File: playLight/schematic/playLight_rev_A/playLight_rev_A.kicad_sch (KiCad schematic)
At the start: 30 parts, among them J1 Conn_01x01, J10 Conn_01x01, J2 Conn_01x01, J3 Conn_01x01, J4 Conn_01x01, J5 Conn_01x01, J6 Conn_01x01, J7 Conn_01x01, J8 Conn_01x01, J9 Conn_01x01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

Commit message: added gerbers added PDF export
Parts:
- R1, R2: value R_US -> 2.2k
- R3: value R_US -> 1k
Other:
- company: (none) -> QuBi
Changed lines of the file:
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@@
 	(title_block
 		(title "gangQin Playlight")
+		(date "20 April 2026")
 		(rev "Rev A")
+		(company "QuBi")
 	)
 	(junction
@@
 			)
 		)
-		(property "Value" "R_US"
+		(property "Value" "2.2k"
 			(at 119.38 64.7699 0)
 			(effects
@@
 			)
 		)
-		(property "Value" "R_US"
+		(property "Value" "2.2k"
 			(at 132.08 64.7699 0)
 			(effects
@@
 			)
 		)
-		(property "Value" "R_US"
+		(property "Value" "1k"
 			(at 173.99 180.3399 0)
 			(effects

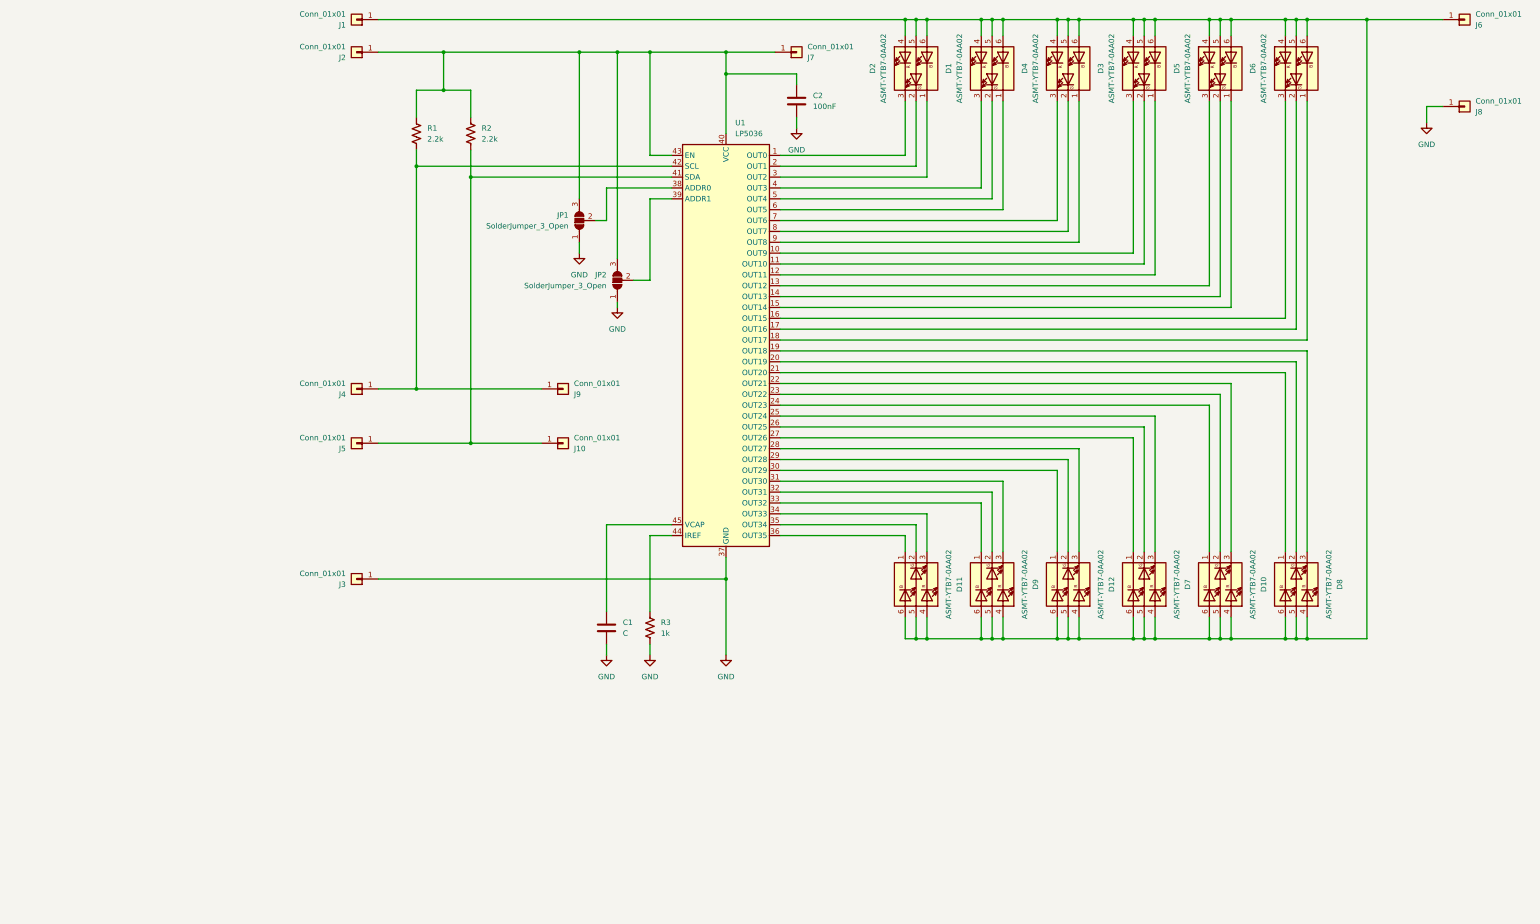
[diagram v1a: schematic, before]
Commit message: added design notes in the schematic minor tweaks in the PCB generated the gerbers accordingly
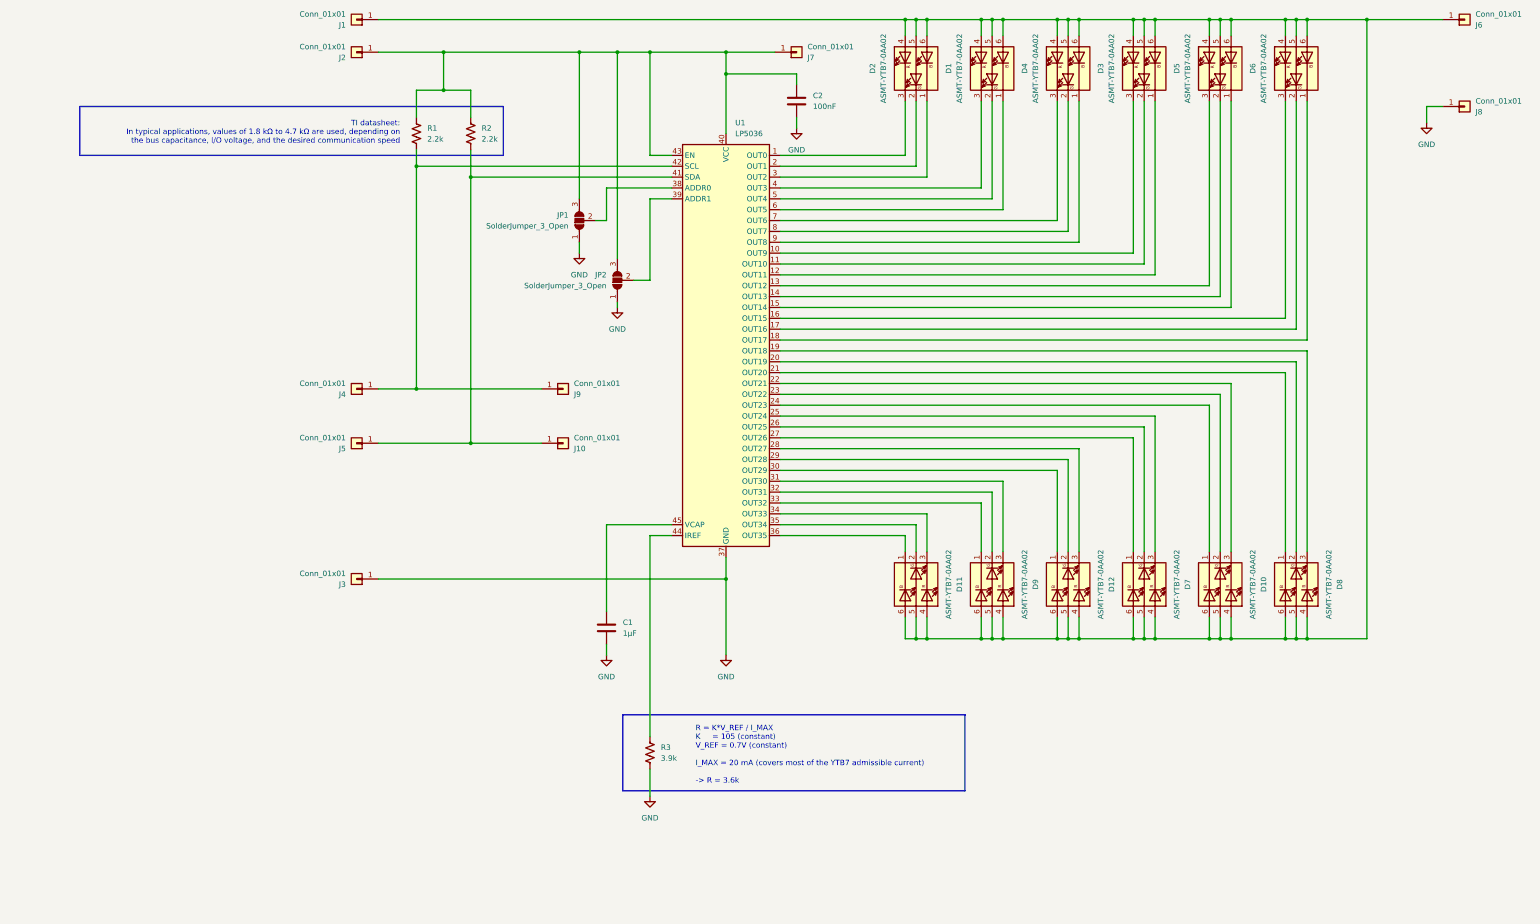
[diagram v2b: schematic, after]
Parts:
- C1: value C -> 1µF
- R3: value 1k -> 3.9k
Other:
- note added: "R = K*V_REF / I_MAX K = 105 (constant) V_REF = 0.7V (constant) I_MAX = 20 mA (covers most of the YTB7 admissible current) -> R = 3.6k"
- note added: "TI datasheet: In typical applications, values of 1.8 kΩ to 4.7 kΩ are used, depending on the bus capacitance, I/O voltage, and the desired communication speed"
- moved on the sheet: R3
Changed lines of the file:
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@@
 		(company "QuBi")
 	)
+	(rectangle
+		(start 38.1 57.15)
+		(end 137.16 68.58)
+		(stroke
+			(width 0)
+			(type default)
+		)
+		(fill
+			(type none)
+		)
+	)
+	(rectangle
+		(start 165.1 199.39)
+		(end 245.11 217.17)
+		(stroke
+			(width 0)
+			(type default)
+		)
+		(fill
+			(type none)
+		)
+	)
+	(text "R = K*V_REF / I_MAX\nK     = 105 (constant)\nV_REF = 0.7V (constant)\n\nI_MAX = 20 mA (covers most of the YTB7 admissible current)\n\n-> R = 3.6k\n"
+		(exclude_from_sim no)
+		(at 182.118 208.788 0)
+		(effects
+			(font
+				(size 1.27 1.27)
+			)
+			(justify left)
+		)
+	)
+	(text "TI datasheet:\nIn typical applications, values of 1.8 kΩ to 4.7 kΩ are used, depending on\nthe bus capacitance, I/O voltage, and the desired communication speed\n"
+		(exclude_from_sim no)
+		(at 113.03 63.246 0)
+		(effects
+			(font
+				(size 1.27 1.27)
+			)
+			(justify right)
+		)
+	)
 	(junction
 		(at 325.12 36.83)
@@
 	(wire
 		(pts
-			(xy 171.45 175.26) (xy 171.45 157.48)
+			(xy 171.45 204.47) (xy 171.45 157.48)
 		)
 		(stroke
@@
 	(wire
 		(pts
-			(xy 171.45 182.88) (xy 171.45 185.42)
+			(xy 171.45 212.09) (xy 171.45 218.44)
 		)
 		(stroke
@@
 	(symbol
 		(lib_id "power:GND")
-		(at 171.45 185.42 0)
+		(at 171.45 218.44 0)
 		(unit 1)
 		(exclude_from_sim no)
@@
 		(fields_autoplaced yes)
 		(property "Reference" "#PWR04"
-			(at 171.45 191.77 0)
+			(at 171.45 224.79 0)
 			(effects
 				(font
@@
 		)
 		(property "Value" "GND"
-			(at 171.45 190.5 0)
+			(at 171.45 223.52 0)
 			(effects
 				(font
@@
 		)
 		(property "Footprint" ""
-			(at 171.45 185.42 0)
+			(at 171.45 218.44 0)
 			(effects
 				(font
@@
 		)
 		(property "Datasheet" ""
-			(at 171.45 185.42 0)
+			(at 171.45 218.44 0)
 			(effects
 				(font
@@
 		)
 		(property "Description" "Power symbol creates a global label with name \"GND\" , ground"
-			(at 171.45 185.42 0)
+			(at 171.45 218.44 0)
 			(effects
 				(font
@@
 			)
 		)
-		(property "Value" "C"
+		(property "Value" "1µF"
 			(at 165.1 180.3399 0)
 			(effects
@@
 	(symbol
 		(lib_id "Device:R_US")
-		(at 171.45 179.07 0)
+		(at 171.45 208.28 0)
 		(unit 1)
 		(exclude_from_sim no)
@@
 		(dnp no)
 		(property "Reference" "R3"
-			(at 173.99 177.7999 0)
+			(at 173.99 207.0099 0)
 			(effects
 				(font
@@
 			)
 		)
-		(property "Value" "1k"
-			(at 173.99 180.3399 0)
+		(property "Value" "3.9k"
+			(at 173.99 209.5499 0)
 			(effects
 				(font
@@
 		)
 		(property "Footprint" "Resistor_SMD:R_0603_1608Metric_Pad0.98x0.95mm_HandSolder"
-			(at 172.466 179.324 90)
+			(at 172.466 208.534 90)
 			(effects
 				(font
@@
 		)
 		(property "Datasheet" "~"
-			(at 171.45 179.07 0)
+			(at 171.45 208.28 0)
 			(effects
 				(font
@@
 		)
 		(property "Description" "Resistor, US symbol"
-			(at 171.45 179.07 0)
+			(at 171.45 208.28 0)
 			(effects
 				(font

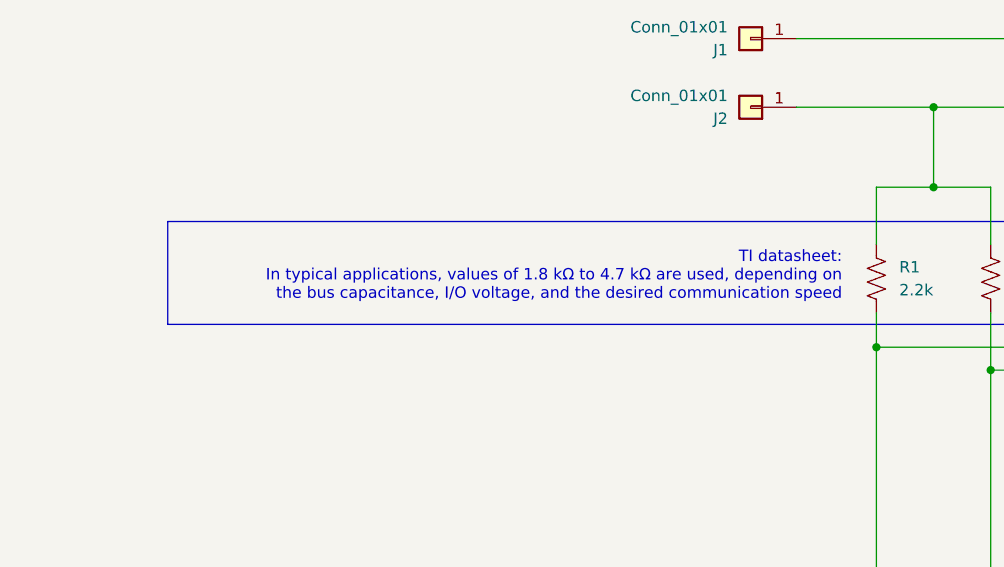
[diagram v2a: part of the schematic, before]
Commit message: changed the LED routing to pass the DRC
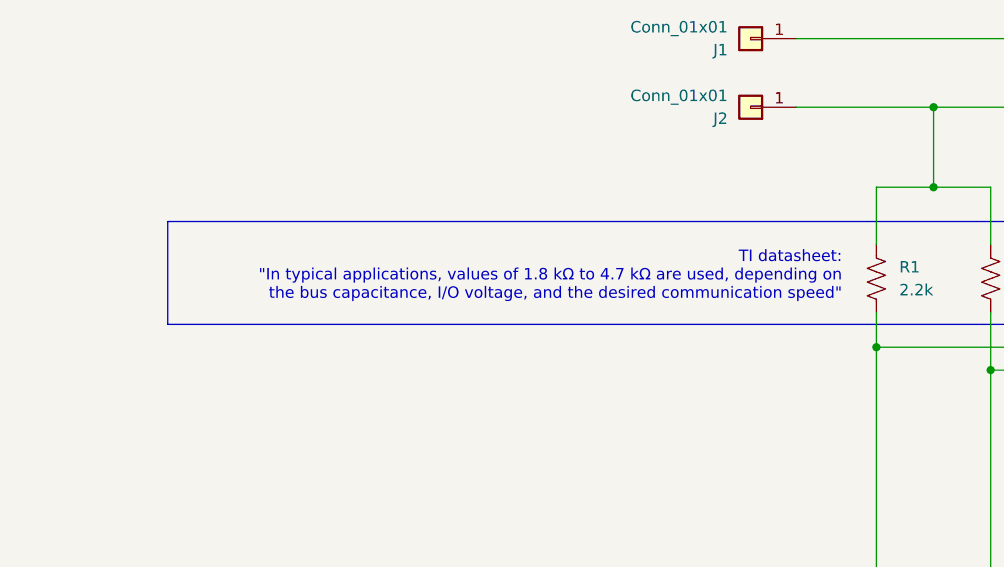
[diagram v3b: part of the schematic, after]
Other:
- note added: "TI datasheet: "In typical applications, values of 1.8 kΩ to 4.7 kΩ are used, depending on the bus capacitance, I/O voltage, and the desired communication speed""
- note removed: "TI datasheet: In typical applications, values of 1.8 kΩ to 4.7 kΩ are used, depending on the bus capacitance, I/O voltage, and the desired communication speed"
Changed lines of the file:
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@@
 		)
 	)
-	(text "TI datasheet:\nIn typical applications, values of 1.8 kΩ to 4.7 kΩ are used, depending on\nthe bus capacitance, I/O voltage, and the desired communication speed\n"
+	(text "TI datasheet:\n\"In typical applications, values of 1.8 kΩ to 4.7 kΩ are used, depending on\nthe bus capacitance, I/O voltage, and the desired communication speed\"\n"
 		(exclude_from_sim no)
 		(at 113.03 63.246 0)

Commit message: added the mounting holes required by JLCPCB
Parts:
- added H1, H2, H3: MountingHole, projectLib_playLight:JLCPCB_Tooling_Hole, symbol Mechanical:MountingHole
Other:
- note added: "JLCPCB tooling holes"
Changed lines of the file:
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@@
 	)
 	(rectangle
+		(start 59.69 209.55)
+		(end 107.95 237.49)
+		(stroke
+			(width 0)
+			(type default)
+		)
+		(fill
+			(type none)
+		)
+	)
+	(rectangle
 		(start 38.1 57.15)
 		(end 137.16 68.58)
@@
 		)
 	)
+	(text "JLCPCB tooling holes"
+		(exclude_from_sim no)
+		(at 85.09 224.536 0)
+		(effects
+			(font
+				(size 1.27 1.27)
+			)
+			(justify left)
+		)
+	)
 	(text "TI datasheet:\n\"In typical applications, values of 1.8 kΩ to 4.7 kΩ are used, depending on\nthe bus capacitance, I/O voltage, and the desired communication speed\"\n"
 		(exclude_from_sim no)
@@
 	)
 	(symbol
+		(lib_id "Mechanical:MountingHole")
+		(at 64.77 232.41 0)
+		(unit 1)
+		(exclude_from_sim no)
+		(in_bom no)
+		(on_board yes)
+		(dnp no)
+		(fields_autoplaced yes)
+		(property "Reference" "H3"
+			(at 67.31 231.1399 0)
+			(effects
+				(font
+					(size 1.27 1.27)
+				)
+				(justify left)
+			)
+		)
+		(property "Value" "MountingHole"
+			(at 67.31 233.6799 0)
+			(effects
+				(font
+					(size 1.27 1.27)
+				)
+				(justify left)
+			)
+		)
+		(property "Footprint" "projectLib_playLight:JLCPCB_Tooling_Hole"
+			(at 64.77 232.41 0)
+			(effects
+				(font
+					(size 1.27 1.27)
+				)
+				(hide yes)
+			)
+		)
+		(property "Datasheet" "~"
+			(at 64.77 232.41 0)
+			(effects
+				(font
+					(size 1.27 1.27)
+				)
+				(hide yes)
+			)
+		)
+		(property "Description" "Mounting Hole without connection"
+			(at 64.77 232.41 0)
+			(effects
+				(font
+					(size 1.27 1.27)
+				)
+				(hide yes)
+			)
+		)
+		(instances
+			(project "playLight_rev_A"
+				(path "/3ef13e95-f986-4ee7-8906-03eb839b39a7"
+					(reference "H3")
+					(unit 1)
+				)
+			)
+		)
+	)
+	(symbol
 		(lib_id "Connector_Generic:Conn_01x01")
 		(at 102.87 44.45 180)
@@
 	)
 	(symbol
+		(lib_id "Mechanical:MountingHole")
+		(at 64.77 214.63 0)
+		(unit 1)
+		(exclude_from_sim no)
+		(in_bom no)
+		(on_board yes)
+		(dnp no)
+		(fields_autoplaced yes)
+		(property "Reference" "H1"
+			(at 67.31 213.3599 0)
+			(effects
+				(font
+					(size 1.27 1.27)
+				)
+				(justify left)
+			)
+		)
+		(property "Value" "MountingHole"
+			(at 67.31 215.8999 0)
+			(effects
+				(font
+					(size 1.27 1.27)
+				)
+				(justify left)
+			)
+		)
+		(property "Footprint" "projectLib_playLight:JLCPCB_Tooling_Hole"
+			(at 64.77 214.63 0)
+			(effects
+				(font
+					(size 1.27 1.27)
+				)
+				(hide yes)
+			)
+		)
+		(property "Datasheet" "~"
+			(at 64.77 214.63 0)
+			(effects
+				(font
+					(size 1.27 1.27)
+				)
+				(hide yes)
+			)
+		)
+		(property "Description" "Mounting Hole without connection"
+			(at 64.77 214.63 0)
+			(effects
+				(font
+					(size 1.27 1.27)
+				)
+				(hide yes)
+			)
+		)
+		(instances
+			(project ""
+				(path "/3ef13e95-f986-4ee7-8906-03eb839b39a7"
+					(reference "H1")
+					(unit 1)
+				)
+			)
+		)
+	)
+	(symbol
 		(lib_id "power:GND")
 		(at 205.74 62.23 0)
@@
 					(unit 1)
 				)
+			)
+		)
+	)
+	(symbol
+		(lib_id "Mechanical:MountingHole")
+		(at 64.77 223.52 0)
+		(unit 1)
+		(exclude_from_sim no)
+		(in_bom no)
+		(on_board yes)
+		(dnp no)
+		(fields_autoplaced yes)
+		(property "Reference" "H2"
+			(at 67.31 222.2499 0)
+			(effects
+				(font
+					(size 1.27 1.27)
+				)
+				(justify left)
+			)
+		)
+		(property "Value" "MountingHole"
+			(at 67.31 224.7899 0)
+			(effects
+				(font
+					(size 1.27 1.27)
+				)
+				(justify left)
+			)
+		)
+		(property "Footprint" "projectLib_playLight:JLCPCB_Tooling_Hole"
+			(at 64.77 223.52 0)
+			(effects
+				(font
+					(size 1.27 1.27)
+				)
+				(hide yes)
+			)
+		)
+		(property "Datasheet" "~"
+			(at 64.77 223.52 0)
+			(effects
+				(font
+					(size 1.27 1.27)
+				)
+				(hide yes)
+			)
+		)
+		(property "Description" "Mounting Hole without connection"
+			(at 64.77 223.52 0)
+			(effects
+				(font
+					(size 1.27 1.27)
+				)
+				(hide yes)
+			)
+		)
+		(instances
+			(project "playLight_rev_A"
+				(path "/3ef13e95-f986-4ee7-8906-03eb839b39a7"
+					(reference "H2")
+					(unit 1)
+				)

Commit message: removed J connectors from BOM added LCSC refs
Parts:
- added H4: MountingHole, projectLib_playLight:JLCPCB_Tooling_Hole, symbol Mechanical:MountingHole
- C1: MPN (none) -> C1712
- C2: MPN (none) -> C1525
- D1, D10, D11, D12, D2, D3, D4, D5, D6, D7, D8, D9: MPN (none) -> C3018544
- J1, J10, J2, J3, J4, J5, J6, J7, J8, J9: now left out of the parts list
- R1, R2, R3: MPN (none) -> C4190
- U1: MPN (none) -> C701961

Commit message: fixed a few LCSC references
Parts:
- C2: MPN C1525 -> C1711
- R3: MPN C4190 -> C23018
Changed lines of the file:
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@@
 			)
 		)
-		(property "MPN" "C1525"
+		(property "MPN" "C1711"
 			(at 205.74 55.88 0)
 			(effects
@@
 			)
 		)
-		(property "MPN" "C4190"
+		(property "MPN" "C23018"
 			(at 171.45 208.28 0)
 			(effects
